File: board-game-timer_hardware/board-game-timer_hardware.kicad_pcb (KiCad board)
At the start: 2 copper layers, 60 x 60 mm, 9 parts, among them J1 JST_conn_rotary_encoder, J2 JST_conn_tm1637, J3 Conn_01x02_Socket, J4 Conn_01x02_Socket

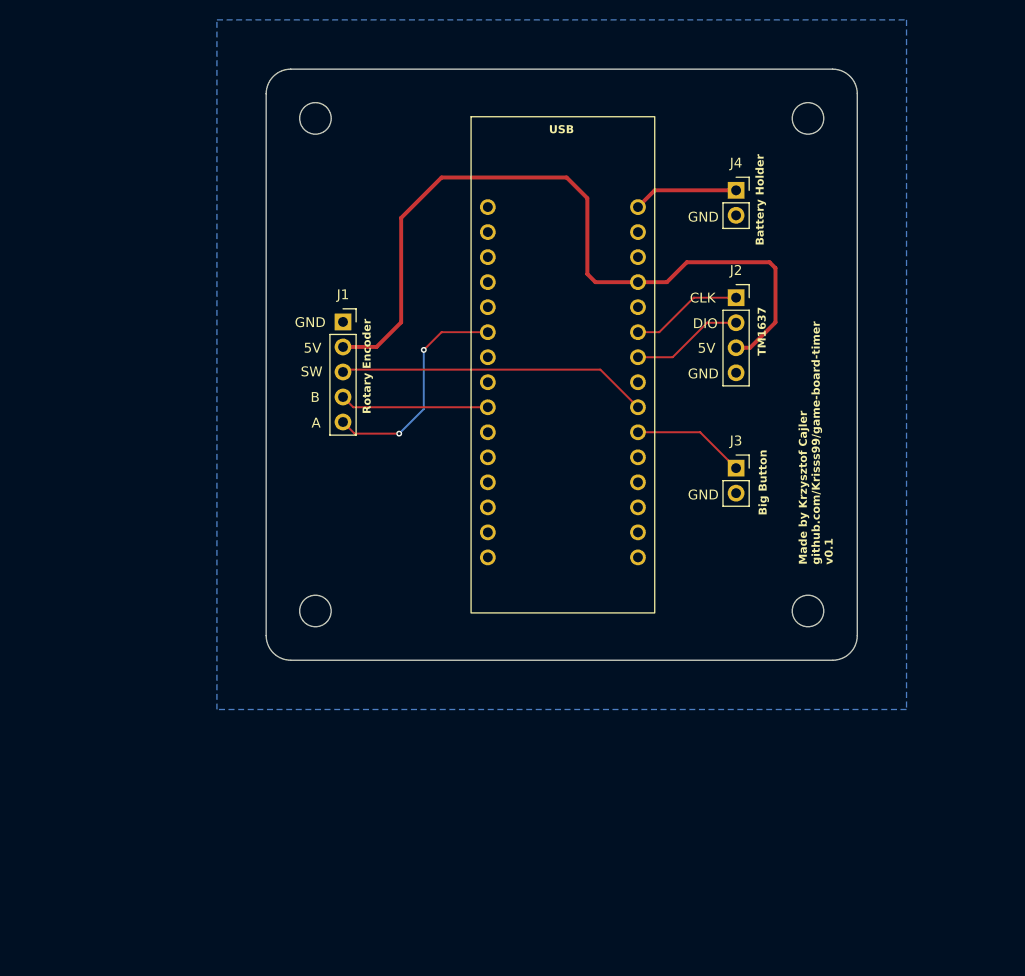
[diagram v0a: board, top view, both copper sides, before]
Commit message: F030f4p6 implementation (#8)
Hardware changes:
New schematic and PCB design around STM32F030F4P6 to keep cost low.

Software changes:
- Rewritten and reconfigured for stm32f030f4
- All the features are the same compared to L432KC
- Removed encoder.c and .h, added TIM implementation
- Blinking effect when selecting time is implemented
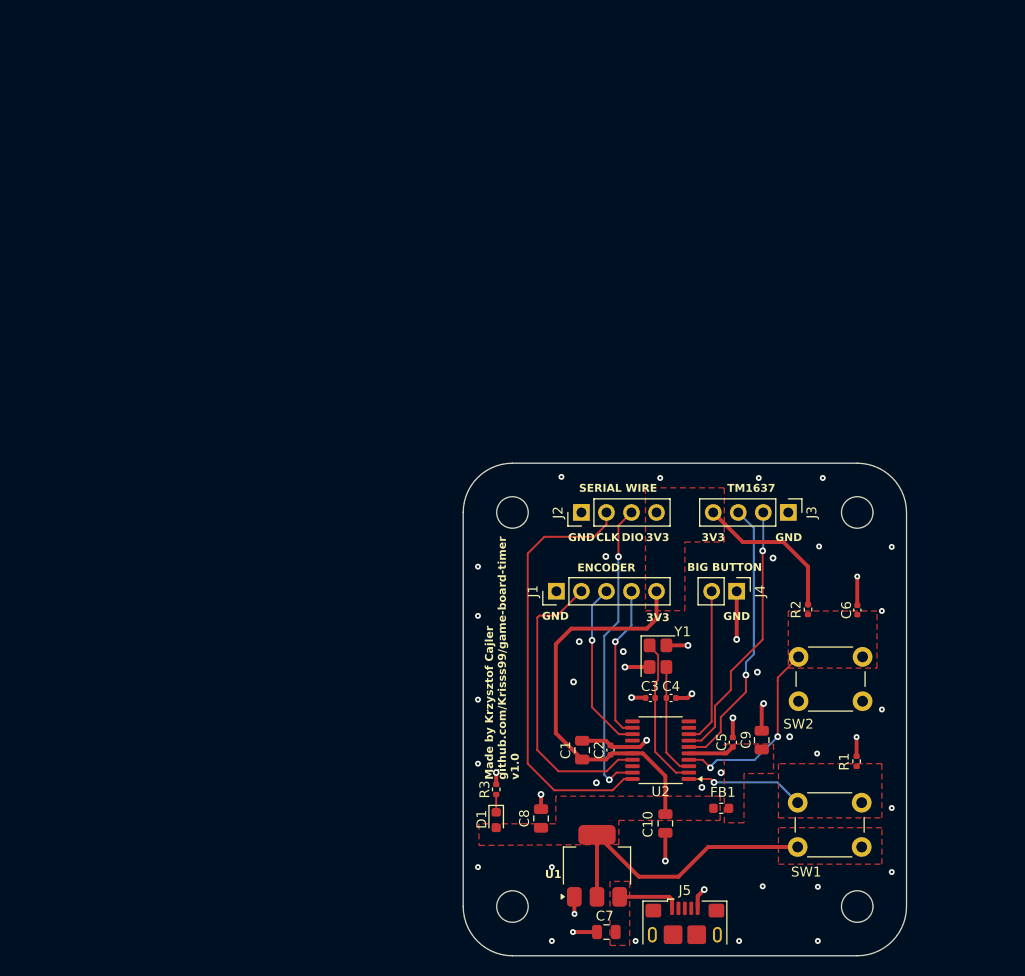
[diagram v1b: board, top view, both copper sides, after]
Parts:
- added C1: 4.7u, Capacitor_SMD:C_0805_2012Metric, F.Cu at (92.1, 89.1)
- added C10: 1u, Capacitor_SMD:C_0805_2012Metric, F.Cu at (100.5, 96.6)
- added C2: 100n, Capacitor_SMD:C_0402_1005Metric, F.Cu at (95.0, 89.1)
- added C3: 10p, Capacitor_SMD:C_0402_1005Metric, F.Cu at (99.0, 83.8)
- added C4: 10p, Capacitor_SMD:C_0402_1005Metric, F.Cu at (101.1, 83.8)
- added C5: 10n, Capacitor_SMD:C_0402_1005Metric, F.Cu at (107.4, 88.3)
- added C6: 100n, Capacitor_SMD:C_0402_1005Metric, F.Cu at (120.0, 74.9)
- added C7: 22u, Capacitor_SMD:C_0805_2012Metric, F.Cu at (94.5, 107.6)
- added C8: 22u, Capacitor_SMD:C_0805_2012Metric, F.Cu at (87.9, 96.1)
- added C9: 1u, Capacitor_SMD:C_0805_2012Metric, F.Cu at (110.3, 88.1)
- added D1: RED, LED_SMD:LED_0603_1608Metric, F.Cu at (83.3, 96.2)
- added FB1: 120R, Inductor_SMD:L_0603_1608Metric, F.Cu at (106.2, 95.0)
- added J5: USB_B_Micro, Connector_USB:USB_Micro-B_Amphenol_10118193-0001LF_Horizontal, F.Cu at (102.5, 107.9)
- added R1: 10k, Resistor_SMD:R_0402_1005Metric, F.Cu at (119.9, 90.3)
- added R2: 10k, Resistor_SMD:R_0402_1005Metric, F.Cu at (115.0, 74.8)
- added R3: 1k5, Resistor_SMD:R_0402_1005Metric, F.Cu at (83.3, 93.1)
- added SW1: SW_B0, Button_Switch_THT:SW_PUSH_6mm, F.Cu at (114.0, 94.5)
- added SW2: SW_RST, Button_Switch_THT:SW_PUSH_6mm, F.Cu at (120.5, 84.2)
- added U2: STM32F030F4Px, Package_SO:TSSOP-20_4.4x6.5mm_P0.65mm, F.Cu at (100.0, 89.1)
- added Y1: 16MHz, Crystal:Crystal_SMD_3225-4Pin_3.2x2.5mm, F.Cu at (99.8, 79.6)
- J1: value JST_conn_rotary_encoder -> Conn_01x05_Pin; footprint Connector_PinSocket_2.54mm:PinSocket_1x05_P2.54mm_Vertical -> Connector_PinHeader_2.54mm:PinHeader_1x05_P2.54mm_Vertical
- J2: value JST_conn_tm1637 -> Conn_01x04_Pin; footprint Connector_PinSocket_2.54mm:PinSocket_1x04_P2.54mm_Vertical -> Connector_PinHeader_2.54mm:PinHeader_1x04_P2.54mm_Vertical
- J3: value Conn_01x02_Socket -> Conn_01x04_Pin; footprint Connector_PinSocket_2.54mm:PinSocket_1x02_P2.54mm_Vertical -> Connector_PinHeader_2.54mm:PinHeader_1x04_P2.54mm_Vertical
- J4: value Conn_01x02_Socket -> Conn_01x02_Pin; footprint Connector_PinSocket_2.54mm:PinSocket_1x02_P2.54mm_Vertical -> Connector_PinHeader_2.54mm:PinHeader_1x02_P2.54mm_Vertical
- U1: value ~ -> AMS1117-3.3; footprint STM32L432KC:STM32L432KC -> Package_TO_SOT_SMD:SOT-223-3_TabPin2
- moved U1 67.8 mm to (93.6, 100.9), turned to 90 degrees
- moved H1 44.7 mm to (85.0, 65.0)
- moved J4 40.7 mm to (107.8, 73.0), turned to -90 degrees
- moved H2 40.3 mm to (120.0, 65.0)
- moved H3 36.1 mm to (85.0, 105.0)
- moved J1 34.9 mm to (89.5, 73.0), turned to 90 degrees
- moved H4 30.4 mm to (120.0, 105.0)
- moved J2 26.9 mm to (92.0, 65.0), turned to 90 degrees
- moved J3 6.95 mm to (113.0, 65.0), turned to -90 degrees
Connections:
- J1 pad 2: +5V -> /ENCODER_SW
- J1 pad 3: encoder_switch -> /ENCODER_B
- J1 pad 4: /encoder_B -> /ENCODER_A
- J1 pad 5: /encoder_A -> +3V3
- J2 pad 1: /CLK -> GND
- J2 pad 2: /DIO -> /SW_CLK
- J2 pad 3: +5V -> /SW_DIO
- J2 pad 4: GND -> +3V3
- J3 pad 1: Net-(J3-Pin_1) -> GND
- J3 pad 2: GND -> /TM1637_DIO
- J4 pad 1: Net-(J4-Pin_1) -> GND
- J4 pad 2: GND -> /big_switch
- U1 pad 1: unconnected-(U1-D1/TX/PA_9-Pad1) -> GND
- U1 pad 2: unconnected-(U1-D0/RX/PA_10-Pad2) -> +3V3
- U1 pad 3: unconnected-(U1-RST-Pad3) -> Net-(J5-VBUS)
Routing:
- net +3V3: track 0.00 -> 86.0 mm
- net +5V: track 77.8 -> 0.00 mm
- net /SW_CLK: track 0.00 -> 44.0 mm
- net GND: track 0.00 -> 41.4 mm, vias 0 -> 49
- net encoder_switch: track 32.4 -> 0.00 mm
- net /SW_DIO: track 0.00 -> 31.1 mm, vias 0 -> 2
- net /ENCODER_SW: track 0.00 -> 30.1 mm
- net /TM1637_CLK: track 0.00 -> 28.2 mm, vias 0 -> 1
- net /TM1637_DIO: track 0.00 -> 27.0 mm, vias 0 -> 1
- net /encoder_A: track 23.0 -> 0.00 mm, vias 2 -> 0
- net RST: track 0.00 -> 19.7 mm, vias 0 -> 2
- net /ENCODER_B: track 0.00 -> 17.6 mm, vias 0 -> 1
- net /big_switch: track 0.00 -> 16.1 mm
- net /ENCODER_A: track 0.00 -> 15.8 mm, vias 0 -> 1
- net /OSC_IN: track 0.00 -> 15.7 mm
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- added copper zone on F.Cu, net +3.3VA
- added copper zone on F.Cu, net +3V3
- added copper zone on F.Cu, net BOOT0
- added copper zone on In1.Cu, net GND
- added copper zone on In2.Cu, net GND
- added copper zone on F.Cu, net Net-(J5-VBUS)
- added copper zone on F.Cu, net RST
- removed copper zone on B.Cu, net GND
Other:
- board size 60 x 60 mm -> 45 x 50 mm
- copper layers 2 -> 4
- board text added: "3V3"
- board text added: "BIG BUTTON"
- board text added: "ENCODER"
- board text added: "Made by Krzysztof Cajler github.com/Krisss99/game-board-timer v1.0"
- board text added: "SERIAL WIRE"
- board text added: "U1"
- board text removed: "5V"
- board text removed: "A"
- board text removed: "B"
- board text removed: "Battery Holder"
- board text removed: "Big Button"
- board text removed: "Made by Krzysztof Cajler github.com/Krisss99/game-board-timer v0.1"
- board text removed: "Rotary Encoder"
- board text removed: "SW"
- board text removed: "USB"

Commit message: PCB v1.1
- Moved encoder, screen on the pcb
- Added buzzer
- Changed layer stackup to SIG/GND/PWR/SIG
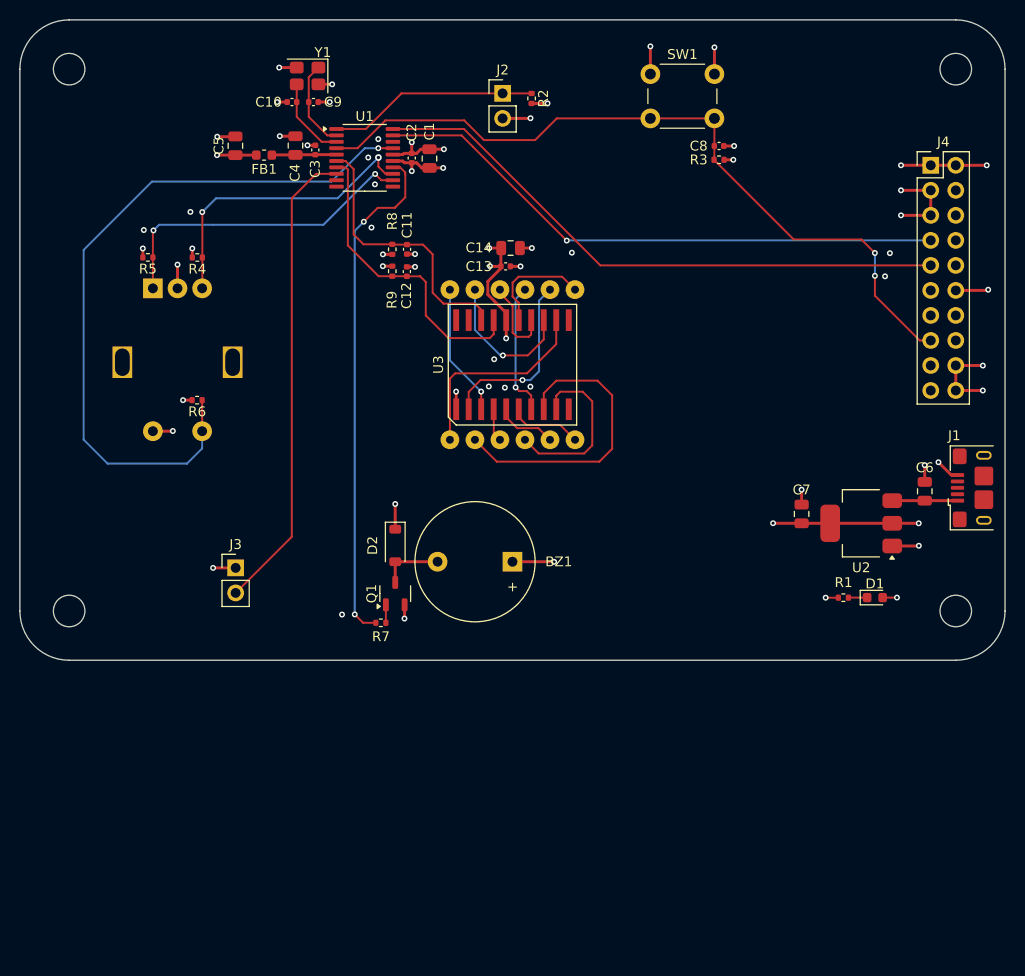
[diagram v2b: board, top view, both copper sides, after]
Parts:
- removed J5: USB_B_Micro, Connector_USB:USB_Micro-B_Amphenol_10118193-0001LF_Horizontal
- added BZ1: Buzzer, Buzzer_Beeper:Buzzer_12x9.5RM7.6, F.Cu at (85.0, 70.0)
- added C11: 100p, Capacitor_SMD:C_0402_1005Metric, F.Cu at (74.3, 38.3)
- added C12: 100p, Capacitor_SMD:C_0402_1005Metric, F.Cu at (74.3, 40.5)
- added C13: 100n, Capacitor_SMD:C_0402_1005Metric, F.Cu at (84.3, 40.0)
- added C14: 10u, Capacitor_SMD:C_0805_2012Metric, F.Cu at (84.8, 38.2)
- added D2: 1N4148W, Diode_SMD:D_SOD-123, F.Cu at (73.1, 68.3)
- added Q1: BC847C,215, Package_TO_SOT_SMD:SOT-23-3, F.Cu at (73.1, 73.2)
- added R4: 10k, Resistor_SMD:R_0402_1005Metric, F.Cu at (53.0, 39.1)
- added R5: 10k, Resistor_SMD:R_0402_1005Metric, F.Cu at (48.0, 39.1)
- added R6: 10k, Resistor_SMD:R_0402_1005Metric, F.Cu at (53.0, 53.6)
- added R7: 470, Resistor_SMD:R_0402_1005Metric, F.Cu at (71.6, 76.2)
- added R8: 10k, Resistor_SMD:R_0402_1005Metric, F.Cu at (72.8, 38.3)
- added R9: 10k, Resistor_SMD:R_0402_1005Metric, F.Cu at (72.8, 40.5)
- added REF**: KiCad-Logo2_6mm_SilkScreen, Symbol:KiCad-Logo2_6mm_SilkScreen, B.Cu at (94.2, 73.2)
- added REF**: OSHW-Logo2_9.8x8mm_SilkScreen, Symbol:OSHW-Logo2_9.8x8mm_SilkScreen, B.Cu at (106.9, 74.0)
- added U3: TM1637, My_own_components:TM1637, F.Cu at (85.0, 50.0)
- added U4: FJ5462AH, My_own_components:ZHIHAO FJ5462AH, B.Cu at (85.0, 50.0)
- C10, C9: value 1u -> 10p; footprint Capacitor_SMD:C_0805_2012Metric -> Capacitor_SMD:C_0402_1005Metric
- C3: value 10p -> 10n
- C4: value 10p -> 1u; footprint Capacitor_SMD:C_0402_1005Metric -> Capacitor_SMD:C_0805_2012Metric
- C5: value 10n -> 1u; footprint Capacitor_SMD:C_0402_1005Metric -> Capacitor_SMD:C_0805_2012Metric
- C6: value 100n -> 22u; footprint Capacitor_SMD:C_0402_1005Metric -> Capacitor_SMD:C_0805_2012Metric
- C8: value 22u -> 100n; footprint Capacitor_SMD:C_0805_2012Metric -> Capacitor_SMD:C_0402_1005Metric
- J1: value Conn_01x05_Pin -> USB_B_Micro; footprint Connector_PinHeader_2.54mm:PinHeader_1x05_P2.54mm_Vertical -> Connector_USB:USB_Micro-B_Amphenol_10118193-0001LF_Horizontal
- J2: value Conn_01x04_Pin -> boot0_jumper; footprint Connector_PinHeader_2.54mm:PinHeader_1x04_P2.54mm_Vertical -> Connector_PinHeader_2.54mm:PinHeader_1x02_P2.54mm_Vertical
- J3: value Conn_01x04_Pin -> BIG_SWITCH_HEADER; footprint Connector_PinHeader_2.54mm:PinHeader_1x04_P2.54mm_Vertical -> Connector_PinHeader_2.54mm:PinHeader_1x02_P2.54mm_Vertical
- J4: value Conn_01x02_Pin -> JTAG_HEADER; footprint Connector_PinHeader_2.54mm:PinHeader_1x02_P2.54mm_Vertical -> Connector_PinHeader_2.54mm:PinHeader_2x10_P2.54mm_Vertical
- R1: value 10k -> 1k5
- R3: value 1k5 -> 10k
- SW1: value SW_B0 -> SW_RST
- SW2: value SW_RST -> EC11E15244G1; footprint Button_Switch_THT:SW_PUSH_6mm -> Rotary_Encoder:RotaryEncoder_Alps_EC11E-Switch_Vertical_H20mm; moved to B.Cu
- U1: value AMS1117-3.3 -> STM32F030F4Px; footprint Package_TO_SOT_SMD:SOT-223-3_TabPin2 -> Package_SO:TSSOP-20_4.4x6.5mm_P0.65mm
- U2: value STM32F030F4Px -> AMS1117-3.3; footprint Package_SO:TSSOP-20_4.4x6.5mm_P0.65mm -> Package_TO_SOT_SMD:SOT-223-3_TabPin2
- moved SW2 83.3 mm to (48.5, 42.2), turned to -90 degrees
- moved C10 82.5 mm to (62.6, 23.3), turned to 180 degrees
- moved FB1 80.9 mm to (59.8, 28.7)
- moved C9 79.2 mm to (64.8, 23.3), turned to 0 degrees
- moved C5 78.8 mm to (56.9, 27.8)
- moved U1 75.6 mm to (70.0, 29.0), turned to 0 degrees
- moved SW1 75.5 mm to (99.0, 20.5)
- moved C8 70.6 mm to (106.0, 27.8), turned to 0 degrees
- moved Y1 68.8 mm to (64.2, 20.7), turned to 180 degrees
- moved C4 67.8 mm to (63.0, 27.8), turned to 90 degrees
- moved R3 67.8 mm to (106.0, 29.2), turned to 180 degrees
- moved C3 65.2 mm to (65.0, 28.2), turned to 90 degrees
- moved H1 63.6 mm to (40.0, 20.0)
- moved C2 63.4 mm to (74.8, 29.0), turned to -90 degrees
- moved C1 62.0 mm to (76.6, 29.1), turned to -90 degrees
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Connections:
- C10 pad 1: +3V3 -> OSC_OUT
- C3 pad 1: /OSC_IN -> +3.3VA
- C4 pad 1: /OSC_OUT -> +3.3VA
- C5 pad 1: +3.3VA -> +3V3
- C6 pad 1: RST -> Net-(J1-VBUS)
- C7 pad 1: Net-(J5-VBUS) -> +3V3
- C8 pad 1: +3V3 -> RST
- C9 pad 1: +3.3VA -> OSC_IN
- J1 pad 1: GND -> Net-(J1-VBUS)
- J1 pad 2: /ENCODER_SW -> unconnected-(J1-D--Pad2)
- J1 pad 3: /ENCODER_B -> unconnected-(J1-D+-Pad3)
- J1 pad 4: /ENCODER_A -> unconnected-(J1-ID-Pad4)
- J1 pad 5: +3V3 -> GND
- J2 pad 1: GND -> BOOT0
- J2 pad 2: /SW_CLK -> +3V3
- J3 pad 2: /TM1637_DIO -> BIG_SWITCH
- J4 pad 1: GND -> +3V3
- J4 pad 2: /big_switch -> +3V3
- R1 pad 1: GND -> /RED-
- R1 pad 2: BOOT0 -> GND
- R2 pad 1: +3V3 -> GND
- R2 pad 2: RST -> BOOT0
- R3 pad 1: /RED- -> +3V3
- R3 pad 2: GND -> RST
- SW1 pad 1: BOOT0 -> GND
- SW1 pad 2: +3V3 -> RST
- U1 pad 1: GND -> BOOT0
- U1 pad 2: +3V3 -> OSC_IN
- U1 pad 3: Net-(J5-VBUS) -> OSC_OUT
- U2 pad 1: BOOT0 -> GND
- U2 pad 2: /OSC_IN -> +3V3
- U2 pad 3: /OSC_OUT -> Net-(J1-VBUS)
- Y1 pad 1: /OSC_IN -> OSC_IN
- Y1 pad 3: /OSC_OUT -> OSC_OUT
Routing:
- net ENC_SW: track 0.00 -> 73.6 mm, vias 0 -> 1
- net SW_CLK: track 0.00 -> 60.3 mm
- net SW_DIO: track 0.00 -> 59.0 mm, vias 0 -> 1
- net RST: track 19.7 -> 77.6 mm
- net BUZZER: track 0.00 -> 52.0 mm, vias 0 -> 2
- net BIG_SWITCH: track 0.00 -> 48.0 mm
- net /SW_CLK: track 44.0 -> 0.00 mm
- net ENC_A: track 0.00 -> 32.9 mm, vias 0 -> 2
- net TM1637_DIO: track 0.00 -> 31.9 mm
- net /SW_DIO: track 31.1 -> 0.00 mm, vias 2 -> 0
- net ENC_B: track 0.00 -> 30.6 mm, vias 0 -> 2
- net Net-(U3-SEG7): track 0.00 -> 30.5 mm
- net /ENCODER_SW: track 30.1 -> 0.00 mm
- net TM1637_CLK: track 0.00 -> 29.0 mm
- net /TM1637_CLK: track 28.2 -> 0.00 mm, vias 1 -> 0
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- added copper zone on In2.Cu, net +3V3
- removed copper zone on F.Cu, net +3.3VA
- removed copper zone on F.Cu, net +3V3
- removed copper zone on F.Cu, net BOOT0
- removed copper zone on In2.Cu, net GND
- removed copper zone on F.Cu, net Net-(J5-VBUS)
- removed copper zone on F.Cu, net RST
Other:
- board size 45 x 50 mm -> 100 x 65 mm
- board text added: "Made by Krzysztof Cajler github.com/Krisss99/game-board-timer v1.1"
- board text removed: "3V3"
- board text removed: "BIG BUTTON"
- board text removed: "CLK"
- board text removed: "DIO"
- board text removed: "ENCODER"
- board text removed: "GND"
- board text removed: "Made by Krzysztof Cajler github.com/Krisss99/game-board-timer v1.0"
- board text removed: "SERIAL WIRE"
- board text removed: "TM1637"
- board text removed: "U1"
